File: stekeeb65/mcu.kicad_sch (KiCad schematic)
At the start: 14 parts, among them IC1 ATMEGA32U4-AU, SW1 SW_Push, Y1 16MHz

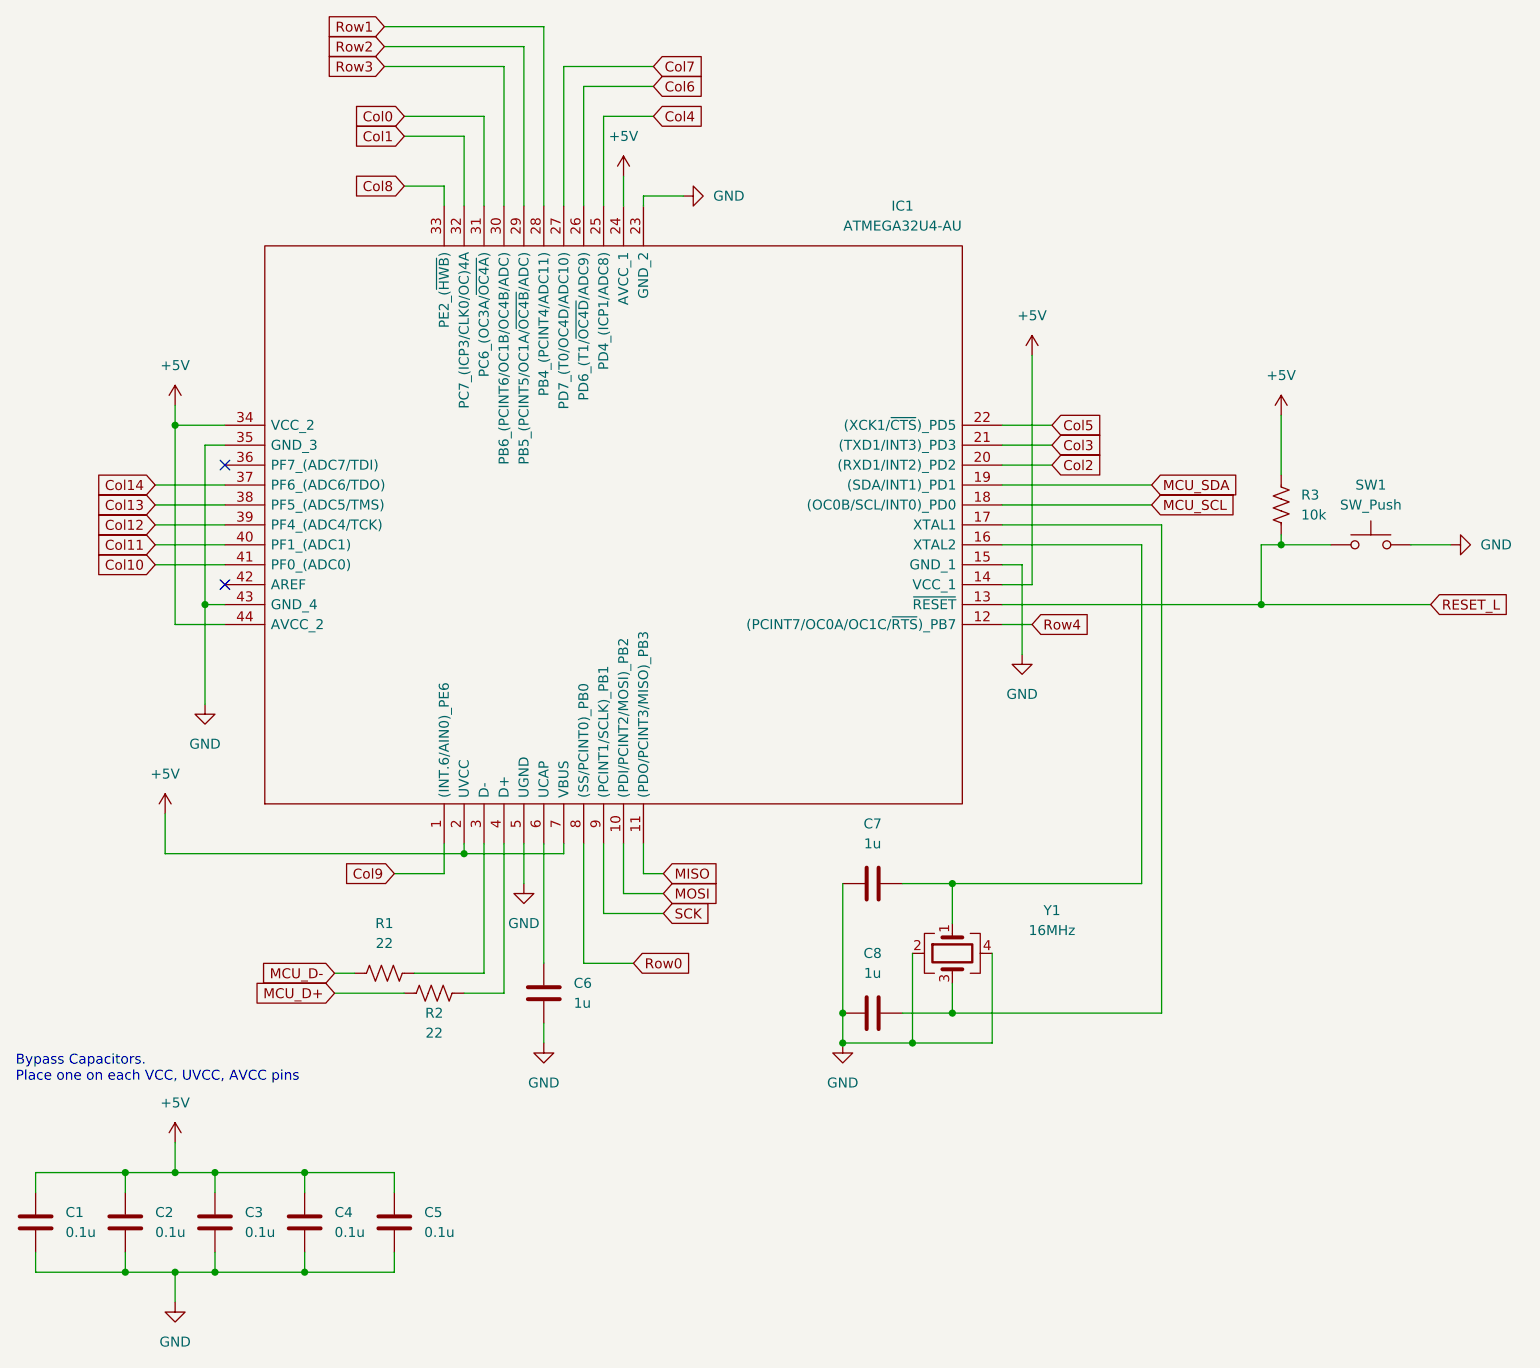
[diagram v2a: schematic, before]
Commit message: Adding key layout with leds
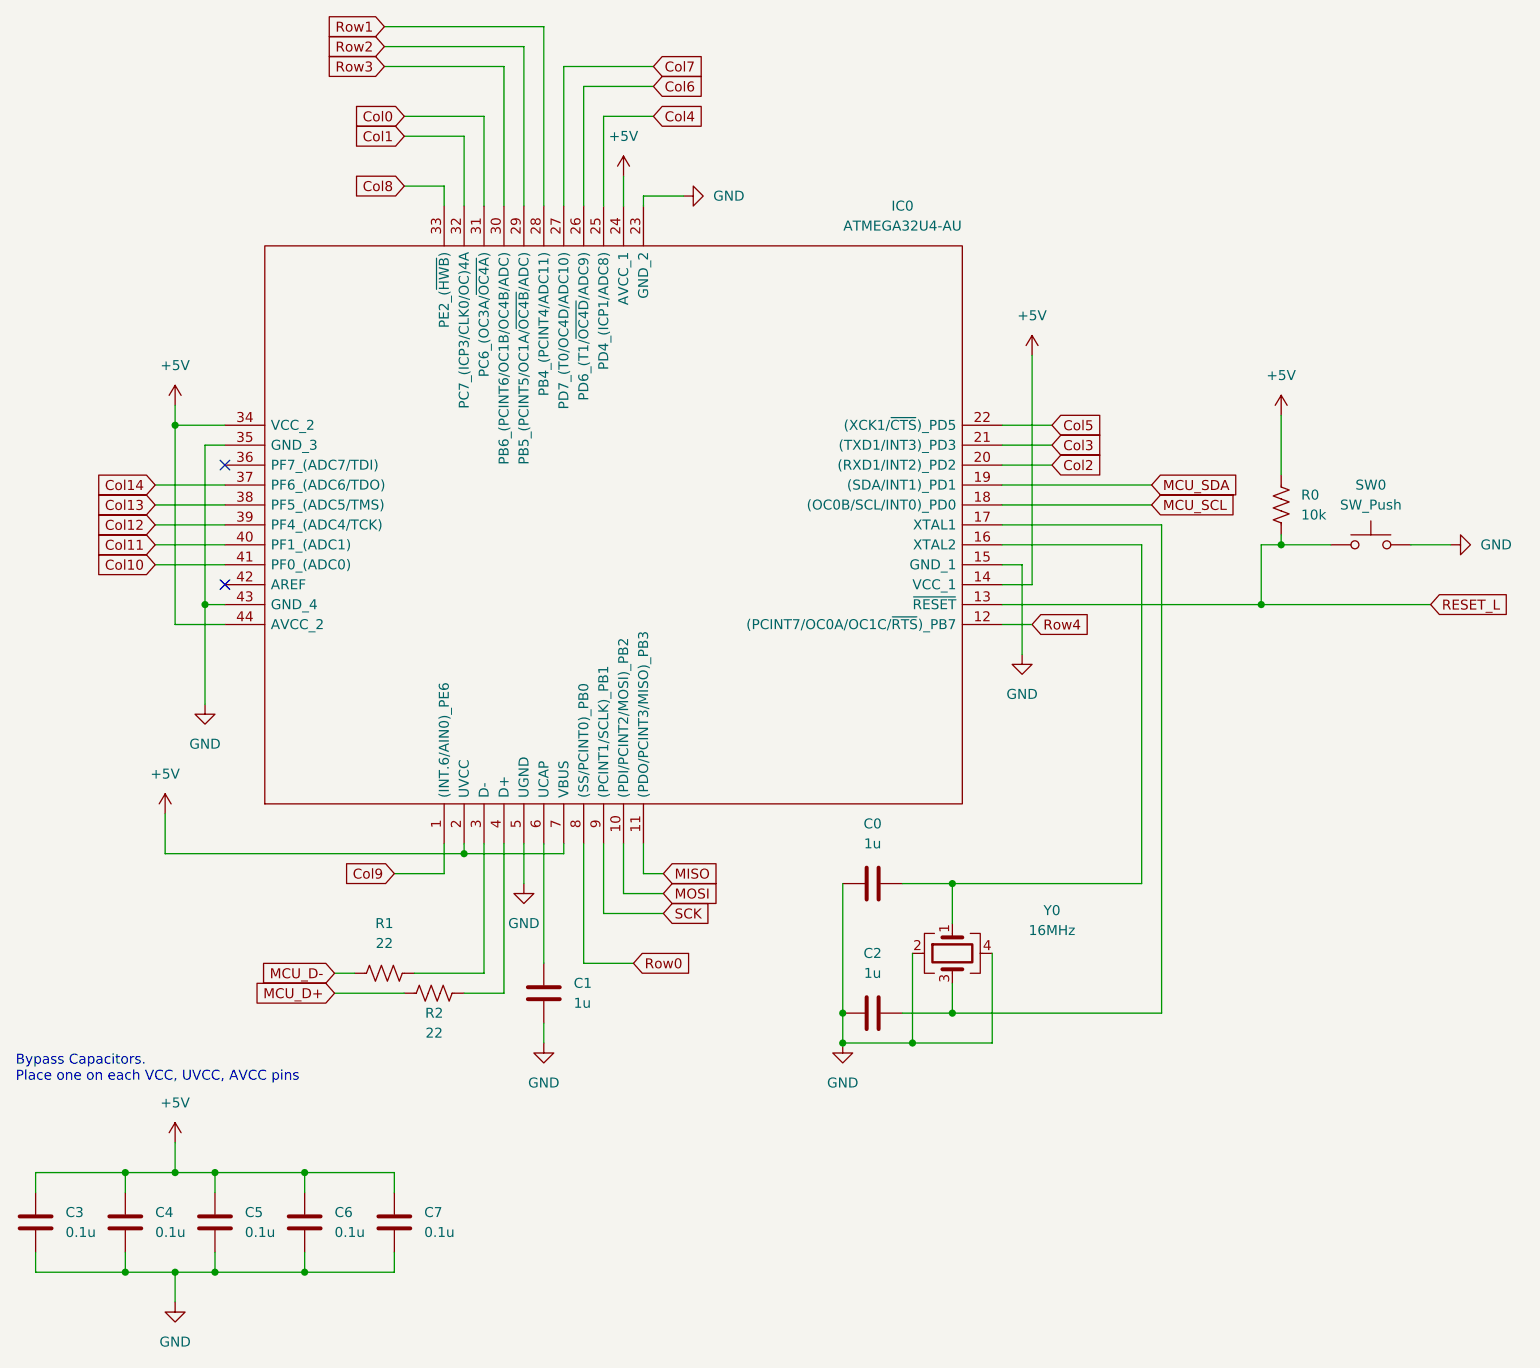
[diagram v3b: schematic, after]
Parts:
- renumbered C7 to C0, C6 to C1, C8 to C2, C1 to C3, C2 to C4, C3 to C5, C4 to C6, C5 to C7, IC1 to IC0, R3 to R0, SW1 to SW0, Y1 to Y0
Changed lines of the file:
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@@
   (symbol (lib_id "Device:R_US") (at 184.15 81.28 180) (unit 1)
     (in_bom yes) (on_board yes) (fields_autoplaced)
-    (property "Reference" "R3" (id 0) (at 186.69 80.0099 0)
+    (property "Reference" "R0" (id 0) (at 186.69 80.0099 0)
       (effects (font (size 1.27 1.27)) (justify right))
     )
@@
   (symbol (lib_id "Device:C") (at 25.4 172.72 0) (unit 1)
     (in_bom yes) (on_board yes) (fields_autoplaced)
-    (property "Reference" "C1" (id 0) (at 29.21 171.4499 0)
+    (property "Reference" "C3" (id 0) (at 29.21 171.4499 0)
       (effects (font (size 1.27 1.27)) (justify left))
     )
@@
   (symbol (lib_id "power:GND") (at 43.18 182.88 0) (unit 1)
     (in_bom yes) (on_board yes) (fields_autoplaced)
-    (property "Reference" "#PWR04" (id 0) (at 43.18 189.23 0)
+    (property "Reference" "#PWR013" (id 0) (at 43.18 189.23 0)
       (effects (font (size 1.27 1.27)) hide)
     )
@@
   (symbol (lib_id "Device:C") (at 71.12 172.72 0) (unit 1)
     (in_bom yes) (on_board yes) (fields_autoplaced)
-    (property "Reference" "C5" (id 0) (at 74.93 171.4499 0)
+    (property "Reference" "C7" (id 0) (at 74.93 171.4499 0)
       (effects (font (size 1.27 1.27)) (justify left))
     )
@@
   (symbol (lib_id "Device:C") (at 59.69 172.72 0) (unit 1)
     (in_bom yes) (on_board yes) (fields_autoplaced)
-    (property "Reference" "C4" (id 0) (at 63.5 171.4499 0)
+    (property "Reference" "C6" (id 0) (at 63.5 171.4499 0)
       (effects (font (size 1.27 1.27)) (justify left))
     )
@@
   (symbol (lib_id "power:GND") (at 151.13 100.33 0) (unit 1)
     (in_bom yes) (on_board yes) (fields_autoplaced)
-    (property "Reference" "#PWR011" (id 0) (at 151.13 106.68 0)
+    (property "Reference" "#PWR06" (id 0) (at 151.13 106.68 0)
       (effects (font (size 1.27 1.27)) hide)
     )
@@
   (symbol (lib_id "power:GND") (at 107.95 41.91 90) (unit 1)
     (in_bom yes) (on_board yes) (fields_autoplaced)
-    (property "Reference" "#PWR09" (id 0) (at 114.3 41.91 0)
+    (property "Reference" "#PWR01" (id 0) (at 114.3 41.91 0)
       (effects (font (size 1.27 1.27)) hide)
     )
@@
   (symbol (lib_id "power:+5V") (at 43.18 68.58 0) (unit 1)
     (in_bom yes) (on_board yes) (fields_autoplaced)
-    (property "Reference" "#PWR02" (id 0) (at 43.18 72.39 0)
+    (property "Reference" "#PWR03" (id 0) (at 43.18 72.39 0)
       (effects (font (size 1.27 1.27)) hide)
     )
@@
   (symbol (lib_id "Switch:SW_Push") (at 195.58 86.36 0) (unit 1)
     (in_bom yes) (on_board yes) (fields_autoplaced)
-    (property "Reference" "SW1" (id 0) (at 195.58 78.74 0))
+    (property "Reference" "SW0" (id 0) (at 195.58 78.74 0))
     (property "Value" "SW_Push" (id 1) (at 195.58 81.28 0))
     (property "Footprint" "random-keyboard-parts:RS187R05A2DSMTRT" (id 2) (at 195.58 81.28 0)
@@
   (symbol (lib_id "power:+5V") (at 100.33 39.37 0) (unit 1)
     (in_bom yes) (on_board yes) (fields_autoplaced)
-    (property "Reference" "#PWR08" (id 0) (at 100.33 43.18 0)
+    (property "Reference" "#PWR00" (id 0) (at 100.33 43.18 0)
       (effects (font (size 1.27 1.27)) hide)
     )
@@
   (symbol (lib_id "SamacSys_Parts:ATMEGA32U4-AU") (at 77.47 124.46 90) (unit 1)
     (in_bom yes) (on_board yes)
-    (property "Reference" "IC1" (id 0) (at 135.89 43.18 90))
+    (property "Reference" "IC0" (id 0) (at 135.89 43.18 90))
     (property "Value" "ATMEGA32U4-AU" (id 1) (at 135.89 45.72 90))
     (property "Footprint" "QFP80P1200X1200X120-44N" (id 2) (at 54.61 46.99 0)
@@
   (symbol (lib_id "power:GND") (at 205.74 86.36 90) (unit 1)
     (in_bom yes) (on_board yes) (fields_autoplaced)
-    (property "Reference" "#PWR014" (id 0) (at 212.09 86.36 0)
+    (property "Reference" "#PWR05" (id 0) (at 212.09 86.36 0)
       (effects (font (size 1.27 1.27)) hide)
     )
@@
   (symbol (lib_id "power:GND") (at 46.99 106.68 0) (unit 1)
     (in_bom yes) (on_board yes) (fields_autoplaced)
-    (property "Reference" "#PWR05" (id 0) (at 46.99 113.03 0)
+    (property "Reference" "#PWR07" (id 0) (at 46.99 113.03 0)
       (effects (font (size 1.27 1.27)) hide)
     )
@@
   (symbol (lib_id "Device:Crystal_GND24") (at 142.24 138.43 90) (mirror x) (unit 1)
     (in_bom yes) (on_board yes) (fields_autoplaced)
-    (property "Reference" "Y1" (id 0) (at 154.94 132.9688 90))
+    (property "Reference" "Y0" (id 0) (at 154.94 132.9688 90))
     (property "Value" "16MHz" (id 1) (at 154.94 135.5088 90))
     (property "Footprint" "Crystal:Crystal_SMD_3225-4Pin_3.2x2.5mm" (id 2) (at 142.24 138.43 0)
@@
   (symbol (lib_id "power:+5V") (at 41.91 120.65 0) (unit 1)
     (in_bom yes) (on_board yes) (fields_autoplaced)
-    (property "Reference" "#PWR01" (id 0) (at 41.91 124.46 0)
+    (property "Reference" "#PWR08" (id 0) (at 41.91 124.46 0)
       (effects (font (size 1.27 1.27)) hide)
     )
@@
   (symbol (lib_id "Device:C") (at 132.08 146.05 270) (unit 1)
     (in_bom yes) (on_board yes) (fields_autoplaced)
-    (property "Reference" "C8" (id 0) (at 132.08 138.43 90))
+    (property "Reference" "C2" (id 0) (at 132.08 138.43 90))
     (property "Value" "1u" (id 1) (at 132.08 140.97 90))
     (property "Footprint" "Capacitor_SMD:C_0805_2012Metric_Pad1.18x1.45mm_HandSolder" (id 2) (at 128.27 147.0152 0)
@@
   (symbol (lib_id "power:GND") (at 90.17 149.86 0) (unit 1)
     (in_bom yes) (on_board yes) (fields_autoplaced)
-    (property "Reference" "#PWR07" (id 0) (at 90.17 156.21 0)
+    (property "Reference" "#PWR010" (id 0) (at 90.17 156.21 0)
       (effects (font (size 1.27 1.27)) hide)
     )
@@
   (symbol (lib_id "power:GND") (at 87.63 129.54 0) (unit 1)
     (in_bom yes) (on_board yes) (fields_autoplaced)
-    (property "Reference" "#PWR06" (id 0) (at 87.63 135.89 0)
+    (property "Reference" "#PWR09" (id 0) (at 87.63 135.89 0)
       (effects (font (size 1.27 1.27)) hide)
     )
@@
   (symbol (lib_id "Device:C") (at 90.17 143.51 0) (unit 1)
     (in_bom yes) (on_board yes) (fields_autoplaced)
-    (property "Reference" "C6" (id 0) (at 93.98 142.2399 0)
+    (property "Reference" "C1" (id 0) (at 93.98 142.2399 0)
       (effects (font (size 1.27 1.27)) (justify left))
     )
@@
   (symbol (lib_id "power:GND") (at 128.27 149.86 0) (unit 1)
     (in_bom yes) (on_board yes) (fields_autoplaced)
-    (property "Reference" "#PWR010" (id 0) (at 128.27 156.21 0)
+    (property "Reference" "#PWR011" (id 0) (at 128.27 156.21 0)
       (effects (font (size 1.27 1.27)) hide)
     )
@@
   (symbol (lib_id "power:+5V") (at 184.15 69.85 0) (unit 1)
     (in_bom yes) (on_board yes) (fields_autoplaced)
-    (property "Reference" "#PWR013" (id 0) (at 184.15 73.66 0)
+    (property "Reference" "#PWR04" (id 0) (at 184.15 73.66 0)
       (effects (font (size 1.27 1.27)) hide)
     )
@@
   (symbol (lib_id "Device:C") (at 36.83 172.72 0) (unit 1)
     (in_bom yes) (on_board yes) (fields_autoplaced)
-    (property "Reference" "C2" (id 0) (at 40.64 171.4499 0)
+    (property "Reference" "C4" (id 0) (at 40.64 171.4499 0)
       (effects (font (size 1.27 1.27)) (justify left))
     )
@@
   (symbol (lib_id "Device:C") (at 132.08 129.54 270) (unit 1)
     (in_bom yes) (on_board yes) (fields_autoplaced)
-    (property "Reference" "C7" (id 0) (at 132.08 121.92 90))
+    (property "Reference" "C0" (id 0) (at 132.08 121.92 90))
     (property "Value" "1u" (id 1) (at 132.08 124.46 90))
     (property "Footprint" "Capacitor_SMD:C_0805_2012Metric_Pad1.18x1.45mm_HandSolder" (id 2) (at 128.27 130.5052 0)
@@
   (symbol (lib_id "power:+5V") (at 152.4 62.23 0) (unit 1)
     (in_bom yes) (on_board yes) (fields_autoplaced)
-    (property "Reference" "#PWR012" (id 0) (at 152.4 66.04 0)
+    (property "Reference" "#PWR02" (id 0) (at 152.4 66.04 0)
       (effects (font (size 1.27 1.27)) hide)
     )
@@
   (symbol (lib_id "Device:C") (at 48.26 172.72 0) (unit 1)
     (in_bom yes) (on_board yes) (fields_autoplaced)
-    (property "Reference" "C3" (id 0) (at 52.07 171.4499 0)
+    (property "Reference" "C5" (id 0) (at 52.07 171.4499 0)
       (effects (font (size 1.27 1.27)) (justify left))
     )
@@
   (symbol (lib_id "power:+5V") (at 43.18 162.56 0) (unit 1)
     (in_bom yes) (on_board yes) (fields_autoplaced)
-    (property "Reference" "#PWR03" (id 0) (at 43.18 166.37 0)
-      (effects (font (size 1.27 1.27)) hide)
-    )
+    (property "Reference" "#PWR012" (id 0) (at 43.18 166.37 0)
+      (effects (font (size 1.27 1.27)) hide)
+    )

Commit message: Adding layout for diodes, LEDs, edge cuts
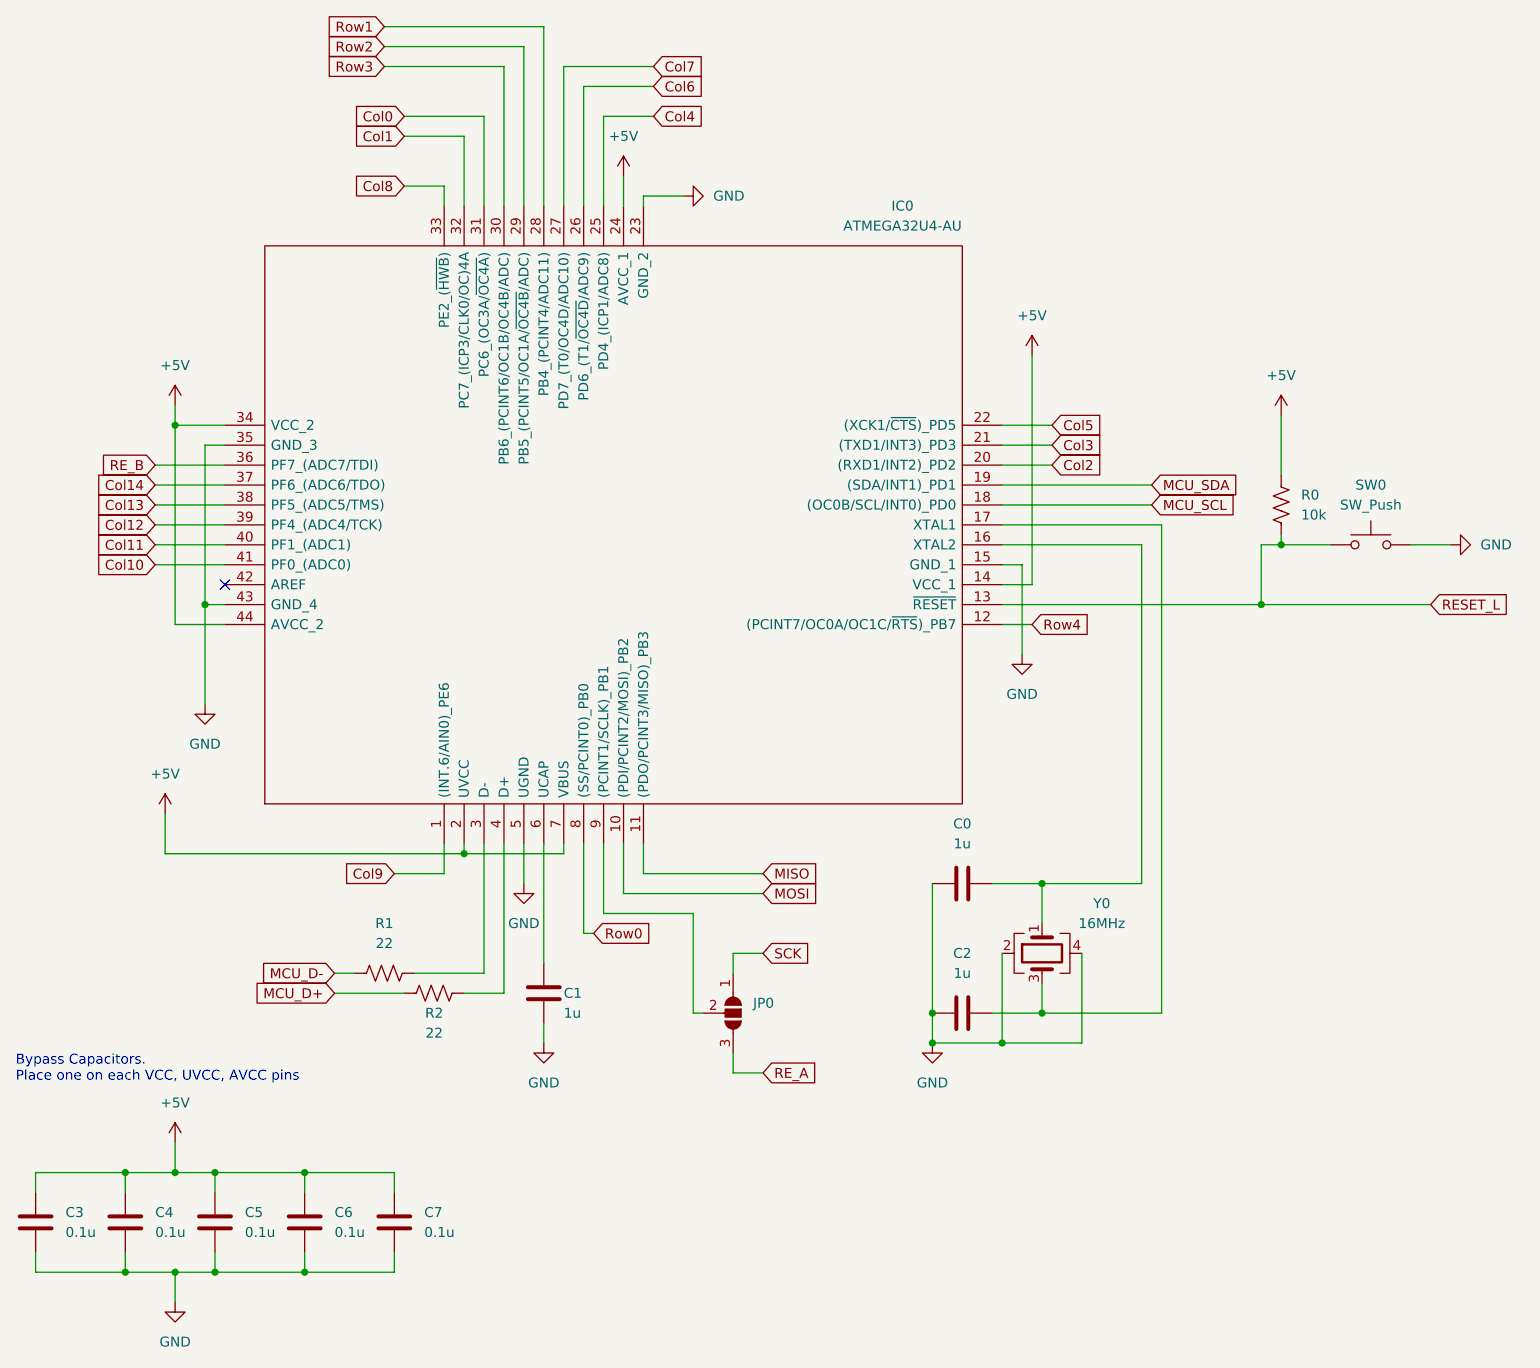
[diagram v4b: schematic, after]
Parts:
- added JP0: SolderJumper_3_Open, Jumper:SolderJumper-3_P1.3mm_Open_RoundedPad1.0x1.5mm, symbol Jumper:SolderJumper_3_Open
- IC0: footprint QFP80P1200X1200X120-44N -> SamacSys_Parts:QFP80P1200X1200X120-44N
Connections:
- net SCK: now also JP0.1 (A); no longer IC0.9 ((PCINT1/SCLK)_PB1)
- net RE_B: now reaches IC0.36 (PF7_(ADC7/TDI))
- new net: IC0.9 ((PCINT1/SCLK)_PB1), JP0.2 (C)
- new net RE_A: JP0.3 (B)
- no-connect marks 2 -> 1
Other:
- moved on the sheet: C0, C2, Y0
